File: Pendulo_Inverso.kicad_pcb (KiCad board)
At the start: 2 copper layers, 53.3 x 63.5 mm, 6 parts, among them IC2 TB6612FNG, U1 LM7805_TO220, U2 ESP32-DEVKITC, U4 MPU-6050-A

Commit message: new file:   Pendulo_Inverso-backups/Pendulo_Inverso-2024-03-22_111232.zip 	new file:   Pendulo_Inverso-backups/Pendulo_Inverso-2024-03-22_111732.zip 	new file:   Pendulo_Inverso-backups/Pendulo_Inverso-2024-03-22_112740.zip 	new file:   Pendulo_Inverso-backups/Pendulo_Inverso-2024-03-22_113249.zip 	modified:   Pendulo_Inverso.kicad_pcb 	modified:   Pendulo_Inverso.kicad_pro 	modified:   Pendulo_Inverso.kicad_sch 	modified:   Pendulo_Inverso.dsn 	modified:   Pendulo_Inverso.kicad_pcb 	modified:   Pendulo_Inverso.kicad_sch 	modified:   Pendulo_Inverso.rules 	modified:   Pendulo_Inverso.ses 	modified:   fp-info-cache
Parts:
- added REF**: MountingHole_2.1mm, MountingHole:MountingHole_2.1mm, F.Cu at (116.8, 78.7)
- added REF**: MountingHole_2.1mm, MountingHole:MountingHole_2.1mm, F.Cu at (167.6, 137.2)
- added REF**: MountingHole_2.1mm, MountingHole:MountingHole_2.1mm, F.Cu at (116.8, 137.2)
- added REF**: MountingHole_2.1mm, MountingHole:MountingHole_2.1mm, F.Cu at (167.6, 78.7)
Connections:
- IC2 pad 1: VM -> unconnected-(IC2-VM1-Pad1)
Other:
- board size 53.3 x 63.5 mm -> 55.9 x 63.5 mm
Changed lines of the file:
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@@
   (net 2 "GND")
   (net 3 "Net-(U1-VO)")
-  (net 4 "VM")
+  (net 4 "unconnected-(IC2-VM1-Pad1)")
   (net 5 "VCC")
   (net 6 "AO1")
@@
       (stroke (width 0.1) (type solid))    )
     (pad "1" thru_hole circle (at 0 0) (size 2.286 2.286) (drill 1) (layers "*.Cu" "*.Mask")
-      (net 4 "VM") (pinfunction "VM1") (pintype "power_in"))
+      (net 4 "unconnected-(IC2-VM1-Pad1)") (pinfunction "VM1") (pintype "power_in+no_connect"))
     (pad "2" thru_hole circle (at 0 2.54) (size 2.286 2.286) (drill 1) (layers "*.Cu" "*.Mask")
       (net 5 "VCC") (pinfunction "VCC") (pintype "power_in"))
@@
       (net 2 "GND") (pinfunction "GND") (pintype "power_in"))
   )
+  (footprint "MountingHole:MountingHole_2.1mm" (layer "F.Cu")
+    (at 116.84 78.74)
+    (descr "Mounting Hole 2.1mm, no annular")
+    (tags "mounting hole 2.1mm no annular")
+    (attr exclude_from_pos_files exclude_from_bom)
+    (fp_text reference "REF**" (at 0 -3.2) (layer "F.SilkS")
+        (effects (font (size 1 1) (thickness 0.15)))
+    )
+    (fp_text value "MountingHole_2.1mm" (at 0 3.2) (layer "F.Fab")
+        (effects (font (size 1 1) (thickness 0.15)))
+    )
+    (fp_text user "${REFERENCE}" (at 0 0) (layer "F.Fab")
+        (effects (font (size 1 1) (thickness 0.15)))
+    )
+    (fp_circle (center 0 0) (end 2.1 0)
+      (stroke (width 0.15) (type solid)) (fill none) (layer "Cmts.User"))
+    (fp_circle (center 0 0) (end 2.35 0)
+      (stroke (width 0.05) (type solid)) (fill none) (layer "F.CrtYd"))
+    (pad "" np_thru_hole circle (at 0 0) (size 2.1 2.1) (drill 2.1) (layers "*.Cu" "*.Mask"))
+  )
+  (footprint "MountingHole:MountingHole_2.1mm" (layer "F.Cu")
+    (at 167.64 137.16)
+    (descr "Mounting Hole 2.1mm, no annular")
+    (tags "mounting hole 2.1mm no annular")
+    (attr exclude_from_pos_files exclude_from_bom)
+    (fp_text reference "REF**" (at 0 -3.2) (layer "F.SilkS")
+        (effects (font (size 1 1) (thickness 0.15)))
+    )
+    (fp_text value "MountingHole_2.1mm" (at 0 3.2) (layer "F.Fab")
+        (effects (font (size 1 1) (thickness 0.15)))
+    )
+    (fp_text user "${REFERENCE}" (at 0 0) (layer "F.Fab")
+        (effects (font (size 1 1) (thickness 0.15)))
+    )
+    (fp_circle (center 0 0) (end 2.1 0)
+      (stroke (width 0.15) (type solid)) (fill none) (layer "Cmts.User"))
+    (fp_circle (center 0 0) (end 2.35 0)
+      (stroke (width 0.05) (type solid)) (fill none) (layer "F.CrtYd"))
+    (pad "" np_thru_hole circle (at 0 0) (size 2.1 2.1) (drill 2.1) (layers "F&B.Cu" "*.Mask"))
+  )
   (footprint "Capacitor_SMD:CP_Elec_3x5.3" (layer "F.Cu")
     (at 161.06 124.69)
@@
       (rotate (xyz 0 0 0))
     )
+  )
+  (footprint "MountingHole:MountingHole_2.1mm" (layer "F.Cu")
+    (at 116.84 137.16)
+    (descr "Mounting Hole 2.1mm, no annular")
+    (tags "mounting hole 2.1mm no annular")
+    (attr exclude_from_pos_files exclude_from_bom)
+    (fp_text reference "REF**" (at 0 -3.2) (layer "F.SilkS")
+        (effects (font (size 1 1) (thickness 0.15)))
+    )
+    (fp_text value "MountingHole_2.1mm" (at 0 3.2) (layer "F.Fab")
+        (effects (font (size 1 1) (thickness 0.15)))
+    )
+    (fp_text user "${REFERENCE}" (at 0 0) (layer "F.Fab")
+        (effects (font (size 1 1) (thickness 0.15)))
+    )
+    (fp_circle (center 0 0) (end 2.1 0)
+      (stroke (width 0.15) (type solid)) (fill none) (layer "Cmts.User"))
+    (fp_circle (center 0 0) (end 2.35 0)
+      (stroke (width 0.05) (type solid)) (fill none) (layer "F.CrtYd"))
+    (pad "" np_thru_hole circle (at 0 0) (size 2.1 2.1) (drill 2.1) (layers "F&B.Cu" "*.Mask"))
   )
   (footprint "Package_TO_SOT_THT:TO-220-3_Vertical" (layer "F.Cu")
@@
       (net 48 "unconnected-(U4-INT-Pad8)") (pinfunction "INT") (pintype "output+no_connect"))
   )
+  (footprint "MountingHole:MountingHole_2.1mm" (layer "F.Cu")
+    (at 167.64 78.74)
+    (descr "Mounting Hole 2.1mm, no annular")
+    (tags "mounting hole 2.1mm no annular")
+    (attr exclude_from_pos_files exclude_from_bom)
+    (fp_text reference "REF**" (at 0 -3.2) (layer "F.SilkS")
+        (effects (font (size 1 1) (thickness 0.15)))
+    )
+    (fp_text value "MountingHole_2.1mm" (at 0 3.2) (layer "F.Fab")
+        (effects (font (size 1 1) (thickness 0.15)))
+    )
+    (fp_text user "${REFERENCE}" (at 0 0) (layer "F.Fab")
+        (effects (font (size 1 1) (thickness 0.15)))
+    )
+    (fp_circle (center 0 0) (end 2.1 0)
+      (stroke (width 0.15) (type solid)) (fill none) (layer "Cmts.User"))
+    (fp_circle (center 0 0) (end 2.35 0)
+      (stroke (width 0.05) (type solid)) (fill none) (layer "F.CrtYd"))
+    (pad "" np_thru_hole circle (at 0 0) (size 2.1 2.1) (drill 2.1) (layers "F&B.Cu" "*.Mask"))
+  )
   (footprint "Capacitor_SMD:CP_Elec_3x5.3" (layer "F.Cu")
     (at 161.06 129.54)
@@
     )
   )
-  (gr_rect (start 114.3 76.2) (end 167.64 139.7)
+  (gr_rect (start 114.3 76.2) (end 170.18 139.7)
     (stroke (width 0.1) (type default)) (fill none) (layer "Edge.Cuts"))
   (gr_text "Miguel Otero Costas\nRobotica USC" (at 149.86 137.16) (layer "F.SilkS")

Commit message: modified:   Pendulo_Inverso.dsn 	modified:   Pendulo_Inverso.kicad_pcb 	modified:   Pendulo_Inverso.kicad_prl 	modified:   Pendulo_Inverso.kicad_sch 	modified:   Pendulo_Inverso.rules 	modified:   Pendulo_Inverso.ses 	modified:   fp-info-cache
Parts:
- removed C3: 0.1uF, Capacitor_SMD:CP_Elec_3x5.3
- removed IC2: TB6612FNG, Mi_Libreria2:TB6612FNG
- removed the REF** at (116.8, 78.7)
- removed the REF** at (167.6, 137.2)
- removed the REF** at (116.8, 137.2)
- removed U2: ESP32-DEVKITC, Mi_Libreria2:MODULE_ESP32-DEVKITC
- removed U4: MPU-6050-A, Mi_Libreria2:MPU6050
- added C1: 0.33uF, Capacitor_SMD:CP_Elec_3x5.3, F.Cu at (171.3, 101.2)
- added ESP32-DEVKITC: ESP32-DEVKITC, Mi_Libreria2:MODULE_ESP32-DEVKITC, F.Cu at (128.2, 107.7)
- added MPU-6050-A: MPU-6050-A, Mi_Libreria2:MPU6050, F.Cu at (149.5, 103.1)
- added Motor1: ~, Mi_Libreria2:Conector_doble, F.Cu at (147.8, 128.7)
- added Motor2: ~, Mi_Libreria2:Conector_doble, F.Cu at (151.9, 128.7)
- added Pilas: ~, Mi_Libreria2:Conector_doble, F.Cu at (156.1, 128.7)
- added REF**: MountingHole_2.1mm, MountingHole:MountingHole_2.1mm, F.Cu at (112.9, 137.5)
- added REF**: MountingHole_2.1mm, MountingHole:MountingHole_2.1mm, F.Cu at (112.9, 74.0)
- added REF**: MountingHole_2.1mm, MountingHole:MountingHole_2.1mm, F.Cu at (176.4, 137.5)
- added TB6612FNG: TB6612FNG, Mi_Libreria2:TB6612FNG, F.Cu at (149.6, 78.8)
- C2: value 0.33uF -> 0.1uF
- moved U1 19.4 mm to (168.8, 124.8)
- moved C2 18.3 mm to (171.3, 109.5)
- moved REF** 9.95 mm to (176.4, 74.0)
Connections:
- C2 pad 1: Net-(U1-VI) -> Net-(U1-VO)
- U1 pad 1: Net-(U1-VI) -> Net-(IC2-VM1)
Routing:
- net GND: track 123.9 -> 222.5 mm, vias 0 -> 1
- net Net-(IC2-VM1): track 0.00 -> 82.6 mm
- net BO1: track 0.00 -> 55.0 mm
- net BO2: track 0.00 -> 50.1 mm
- net AO2: track 0.00 -> 47.4 mm
- net AO1: track 0.00 -> 45.4 mm
- net AIN1: track 98.1 -> 53.5 mm
- net VCC: track 52.3 -> 92.7 mm
- net Net-(U1-VI): track 30.7 -> 0.00 mm, vias 1 -> 0
- net Net-(U1-VO): track 51.7 -> 82.0 mm
- net BIN1: track 111.5 -> 86.0 mm
- net AIN2: track 105.1 -> 94.3 mm
- net BIN2: track 46.3 -> 37.9 mm
- net Net-(U2-IO22): track 19.0 -> 21.8 mm
- net Net-(U2-IO21): track 13.9 -> 16.7 mm
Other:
- board size 55.9 x 63.5 mm -> 73.7 x 73.7 mm
- board text added: "Miguel Otero Costas USC"
- board text removed: "Miguel Otero Costas Robotica USC"

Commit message: new file:   Pendulo_Inverso-backups/Pendulo_Inverso-2024-04-04_134628.zip 	modified:   Pendulo_Inverso.kicad_pcb 	modified:   Pendulo_Inverso.kicad_prl 	modified:   Pendulo_Inverso.kicad_pro 	modified:   Pendulo_Inverso.kicad_sch 	modified:   fp-info-cache
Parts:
- removed C1: 0.33uF, Capacitor_SMD:CP_Elec_3x5.3
- removed ESP32-DEVKITC: ESP32-DEVKITC, Mi_Libreria2:MODULE_ESP32-DEVKITC
- removed MPU-6050-A: MPU-6050-A, Mi_Libreria2:MPU6050
- removed Pilas: ~, Mi_Libreria2:Conector_doble
- removed the REF** at (112.9, 137.5)
- removed the REF** at (112.9, 74.0)
- removed the REF** at (176.4, 137.5)
- removed the REF** at (176.4, 74.0)
- removed TB6612FNG: TB6612FNG, Mi_Libreria2:TB6612FNG
- added C3: 0.1uF, Capacitor_THT:CP_Radial_D8.0mm_P3.50mm, F.Cu at (161.6, 129.5)
- added IC2: TB6612FNG, Mi_Libreria2:TB6612FNG, F.Cu at (170.2, 119.4)
- added Pilas1: ~, Mi_Libreria2:Conector_doble, F.Cu at (177.8, 120.8)
- added REF**: MountingHole_2.1mm, MountingHole:MountingHole_2.1mm, F.Cu at (114.3, 132.1)
- added REF**: MountingHole_2.1mm, MountingHole:MountingHole_2.1mm, F.Cu at (180.3, 81.3)
- added REF**: MountingHole_2.1mm, MountingHole:MountingHole_2.1mm, F.Cu at (180.3, 132.1)
- added REF**: MountingHole_2.1mm, MountingHole:MountingHole_2.1mm, F.Cu at (114.3, 81.3)
- added U2: ESP32-DEVKITC, Mi_Libreria2:MODULE_ESP32-DEVKITC, F.Cu at (132.1, 110.6)
- added U4: MPU-6050-A, Mi_Libreria2:MPU6050, F.Cu at (156.3, 79.9)
- C2: value 0.1uF -> 0.33uF; footprint Capacitor_SMD:CP_Elec_3x5.3 -> Capacitor_THT:CP_Radial_D8.0mm_P3.50mm
- moved Motor2 34.0 mm to (177.8, 106.7), turned to 180 degrees
- moved Motor1 32.8 mm to (177.8, 115.4), turned to 180 degrees
- moved C2 27.5 mm to (152.4, 129.5)
- moved U1 8.30 mm to (172.7, 132.1), turned to 90 degrees
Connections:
- C2 pad 1: Net-(U1-VO) -> Net-(IC2-VM1)
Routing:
- net GND: track 222.5 -> 0.00 mm, vias 1 -> 0
- net AIN2: track 94.3 -> 13.2 mm
- net BIN1: track 86.0 -> 13.2 mm
- net BO1: track 55.0 -> 8.18 mm
- net AIN1: track 53.5 -> 11.0 mm
- net BO2: track 50.1 -> 8.66 mm
- net AO2: track 47.4 -> 8.11 mm
- net Net-(IC2-VM1): track 82.6 -> 45.0 mm
- net AO1: track 45.4 -> 8.58 mm
- net BIN2: track 37.9 -> 13.2 mm
- net Net-(U1-VO): track 82.0 -> 59.1 mm
- net PWMB: track 29.2 -> 13.2 mm
- net Net-(U2-IO22): track 21.8 -> 14.7 mm
- net VCC: track 92.7 -> 87.9 mm
- net Net-(U2-IO21): track 16.7 -> 17.6 mm
- added copper zone on B.Cu, net GND
- added copper zone on F.Cu, net GND
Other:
- board size 73.7 x 73.7 mm -> 78.7 x 63.5 mm

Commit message: deleted:    Pendulo_Inverso-backups/Pendulo_Inverso-2024-04-04_113047.zip 	deleted:    Pendulo_Inverso-backups/Pendulo_Inverso-2024-04-04_130756.zip 	deleted:    Pendulo_Inverso-backups/Pendulo_Inverso-2024-04-04_131500.zip 	deleted:    Pendulo_Inverso-backups/Pendulo_Inverso-2024-04-04_132033.zip 	deleted:    Pendulo_Inverso-backups/Pendulo_Inverso-2024-04-04_133114.zip 	deleted:    Pendulo_Inverso-backups/Pendulo_Inverso-2024-04-04_134628.zip 	new file:   Pendulo_Inverso-backups/Pendulo_Inverso-2024-04-04_183334.zip 	new file:   Pendulo_Inverso-backups/Pendulo_Inverso-2024-04-04_183941.zip 	new file:   Pendulo_Inverso-backups/Pendulo_Inverso-2024-04-04_185122.zip 	new file:   Pendulo_Inverso-backups/Pendulo_Inverso-2024-04-04_190246.zip 	new file:   Pendulo_Inverso-backups/Pendulo_Inverso-2024-04-04_190834.zip 	new file:   Pendulo_Inverso-backups/Pendulo_Inverso-2024-04-04_191513.zip 	modified:   Pendulo_Inverso.kicad_pcb 	modified:   Pendulo_Inverso.kicad_prl 	modified:   Pendulo_Inverso.kicad_pro 	modified:   fp-info-cache
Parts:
- removed the REF** at (114.3, 132.1)
- removed the REF** at (180.3, 81.3)
- removed the REF** at (180.3, 132.1)
- removed the REF** at (114.3, 81.3)
- added REF**: MountingHole_3.2mm_M3, MountingHole:MountingHole_3.2mm_M3, F.Cu at (114.3, 132.1)
- added REF**: MountingHole_3.2mm_M3, MountingHole:MountingHole_3.2mm_M3, F.Cu at (180.3, 132.1)
- added REF**: MountingHole_3.2mm_M3, MountingHole:MountingHole_3.2mm_M3, F.Cu at (114.3, 81.3)
- added REF**: MountingHole_3.2mm_M3, MountingHole:MountingHole_3.2mm_M3, F.Cu at (180.3, 81.3)
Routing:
- net Net-(IC2-VM1): track 45.0 -> 46.7 mm
- net BO2: track 8.66 -> 8.02 mm

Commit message: deleted:    Pendulo_Inverso-backups/Pendulo_Inverso-2024-03-22_111232.zip 	new file:   Pendulo_Inverso-backups/Pendulo_Inverso-2024-04-06_125540.zip 	new file:   Pendulo_Inverso-backups/Pendulo_Inverso-2024-04-11_225156.zip 	new file:   Pendulo_Inverso-backups/Pendulo_Inverso-2024-04-11_230001.zip 	new file:   Pendulo_Inverso-backups/Pendulo_Inverso-2024-04-11_230555.zip 	modified:   Pendulo_Inverso.kicad_pcb 	modified:   Pendulo_Inverso.kicad_prl 	modified:   Pendulo_Inverso.kicad_sch
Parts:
- Motor1, Motor2, Pilas1: footprint Mi_Libreria2:Conector_doble -> TerminalBlock_Phoenix:TerminalBlock_Phoenix_MKDS-1,5-2_1x02_P5.00mm_Horizontal
- moved Motor2 10.5 mm to (180.3, 96.5), turned to 90 degrees
- moved Motor1 6.80 mm to (180.3, 109.1), turned to 90 degrees
- moved Pilas1 2.75 mm to (180.3, 121.8), turned to 90 degrees
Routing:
- net BO2: track 8.02 -> 25.2 mm
- net BO1: track 7.83 -> 15.7 mm
- net AO1: track 8.27 -> 13.1 mm
- net AO2: track 7.80 -> 12.1 mm
- net Net-(IC2-VM1): track 46.7 -> 50.9 mm

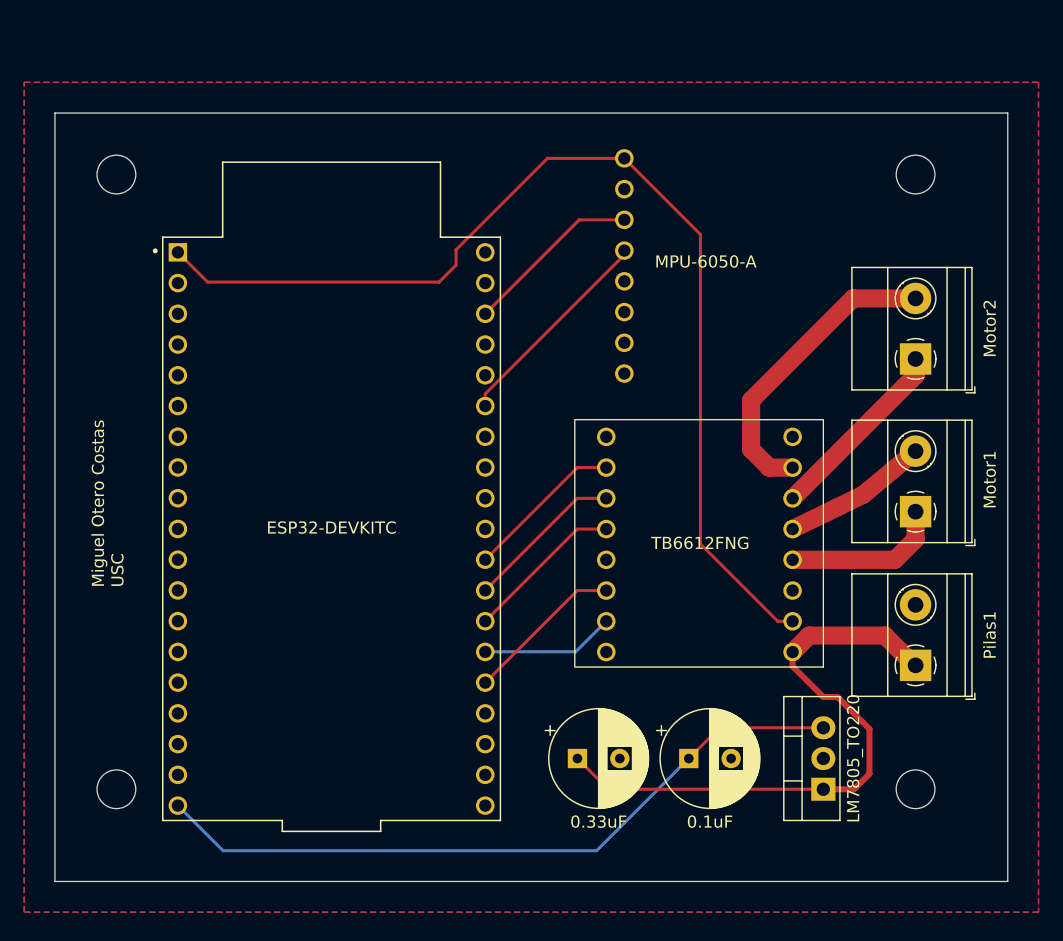
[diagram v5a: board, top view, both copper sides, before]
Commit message: deleted:    Pendulo_Inverso-backups/Pendulo_Inverso-2024-03-22_111732.zip 	deleted:    Pendulo_Inverso-backups/Pendulo_Inverso-2024-03-22_112740.zip 	deleted:    Pendulo_Inverso-backups/Pendulo_Inverso-2024-03-22_113249.zip 	deleted:    Pendulo_Inverso-backups/Pendulo_Inverso-2024-03-27_223923.zip 	deleted:    Pendulo_Inverso-backups/Pendulo_Inverso-2024-03-27_224638.zip 	deleted:    Pendulo_Inverso-backups/Pendulo_Inverso-2024-03-28_220812.zip 	deleted:    Pendulo_Inverso-backups/Pendulo_Inverso-2024-03-28_221557.zip 	deleted:    Pendulo_Inverso-backups/Pendulo_Inverso-2024-03-28_233514.zip 	deleted:    Pendulo_Inverso-backups/Pendulo_Inverso-2024-03-28_234430.zip 	deleted:    Pendulo_Inverso-backups/Pendulo_Inverso-2024-03-28_235840.zip 	deleted:    Pendulo_Inverso-backups/Pendulo_Inverso-2024-03-29_000846.zip 	new file:   Pendulo_Inverso-backups/Pendulo_Inverso-2024-04-14_230244.zip 	new file:   Pendulo_Inverso-backups/Pendulo_Inverso-2024-04-16_180955.zip 	new file:   Pendulo_Inverso-backups/Pendulo_Inverso-2024-04-16_182056.zip 	new file:   Pendulo_Inverso-backups/Pendulo_Inverso-2024-04-16_184932.zip 	new file:   Pendulo_Inverso-backups/Pendulo_Inverso-2024-04-18_112053.zip 	new file:   Pendulo_Inverso-backups/Pendulo_Inverso-2024-04-18_114750.zip 	new file:   Pendulo_Inverso-backups/Pendulo_Inverso-2024-04-18_125733.zip 	new file:   Pendulo_Inverso-backups/Pendulo_Inverso-2024-04-18_130245.zip 	new file:   Pendulo_Inverso-backups/Pendulo_Inverso-2024-04-18_130831.zip 	new file:   Pendulo_Inverso-backups/Pendulo_Inverso-2024-04-18_133403.zip 	modified:   Pendulo_Inverso.kicad_pcb 	modified:   Pendulo_Inverso.kicad_prl 	modified:   Pendulo_Inverso.kicad_sch 	modified:   fp-info-cache
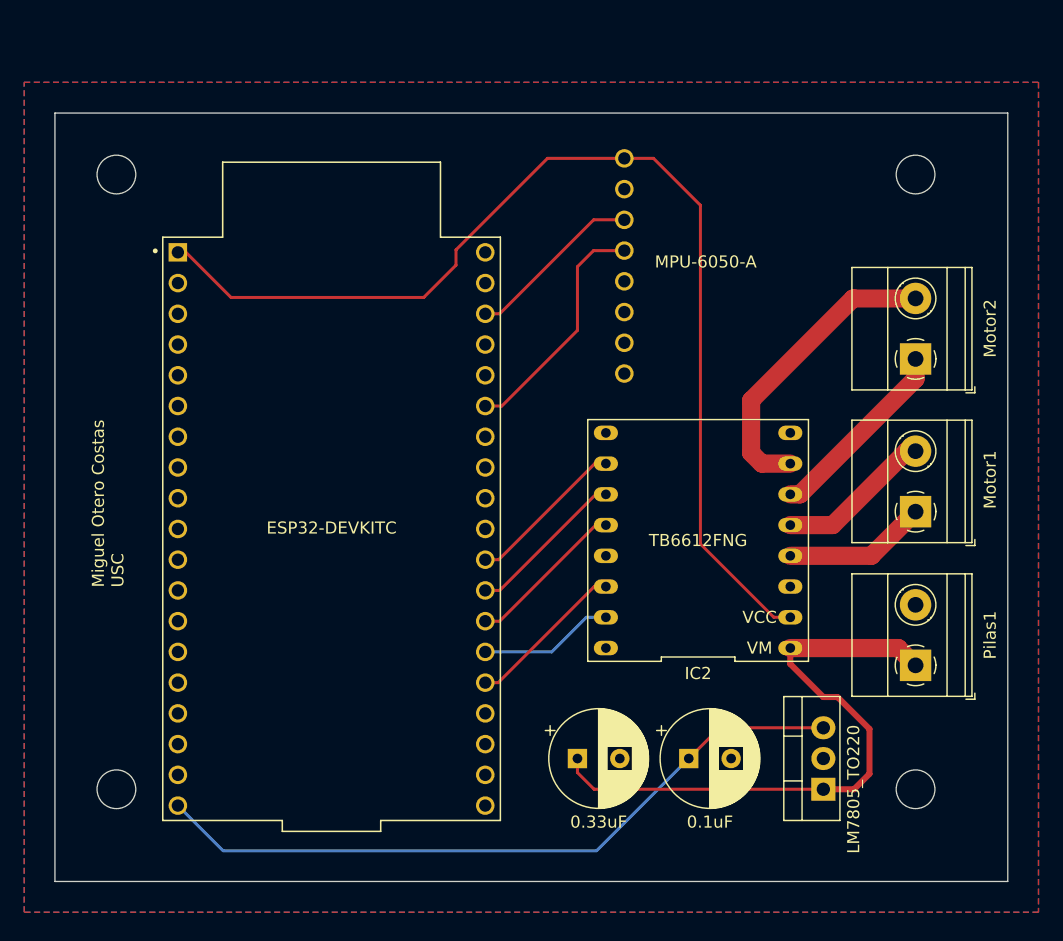
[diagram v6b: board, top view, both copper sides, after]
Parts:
- IC2: footprint Mi_Libreria2:TB6612FNG -> Mi_Libreria2:TB6612FngSparkfun
- moved IC2 14.8 mm to (161.1, 107.7)
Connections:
- IC2 pad 10: AIN1 -> PWMB
- IC2 pad 11: AIN2 -> BIN2
- IC2 pad 12: STBY -> BIN1
- IC2 pad 13: BIN1 -> STBY
- IC2 pad 14: BIN2 -> AIN2
- IC2 pad 15: PWMB -> AIN1
- IC2 pad 16: GND -> PWMA
- IC2 pad 9: PWMA -> GND
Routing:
- net Net-(U2-IO21): track 17.6 -> 19.9 mm
- net VCC: track 87.6 -> 89.8 mm
- net AO1: track 13.1 -> 11.9 mm
- net AO2: track 12.1 -> 12.9 mm
